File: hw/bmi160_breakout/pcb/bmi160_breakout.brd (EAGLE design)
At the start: 10 x 12 mm, 5 parts, among them CON1 B4B-ZR, U1 BMI160LGA14

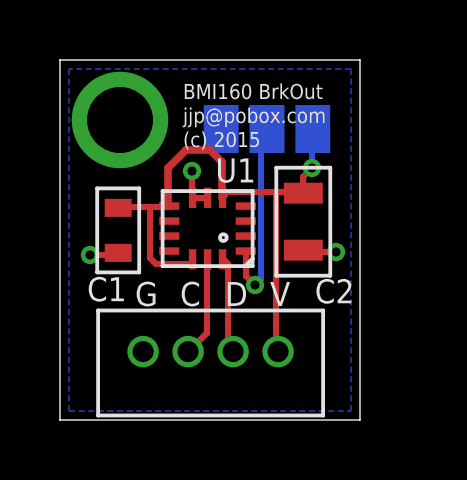
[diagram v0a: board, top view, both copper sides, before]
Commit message: bmi160 breakout: Update primary connector to 0.1" header, as it barely makes the board bigger but makes it a lot more convenient.
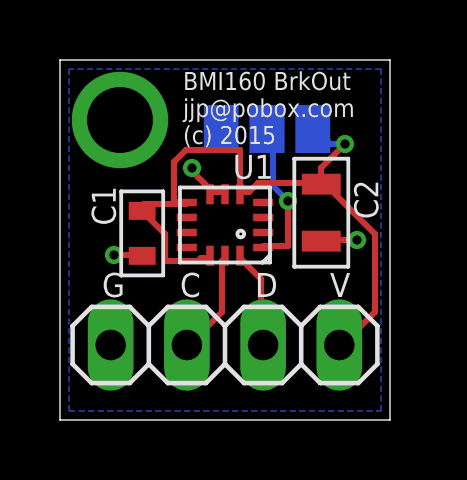
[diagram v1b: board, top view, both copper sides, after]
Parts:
- removed CON1: B4B-ZR, bmi160_breakout:B4B-ZR
- added JP1: (no value), pinhead:1X04
- moved C1 0.81 mm to (2.74, 6.22)
- moved C2 0.67 mm to (8.71, 6.91)
- moved U1 0.59 mm to (5.50, 6.50)
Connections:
- net GND: now also JP1.4; no longer CON1.4
- net SCL: now also JP1.3; no longer CON1.3
- net SDA: now also JP1.2; no longer CON1.2
- net VDD: now also JP1.1; no longer CON1.1
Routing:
- net VDD: track 20.3 -> 23.2 mm
- net N$1: track 6.74 -> 5.16 mm
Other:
- board size 10 x 12 mm -> 11 x 12 mm
